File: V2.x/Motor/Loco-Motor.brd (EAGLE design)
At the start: 43.2 x 34.3 mm, 48 parts, among them IC1 Atmega 328-P, IC2 MCP2515, IC3 LM340MP-05, Q1 8MHz, Q2 16MHz

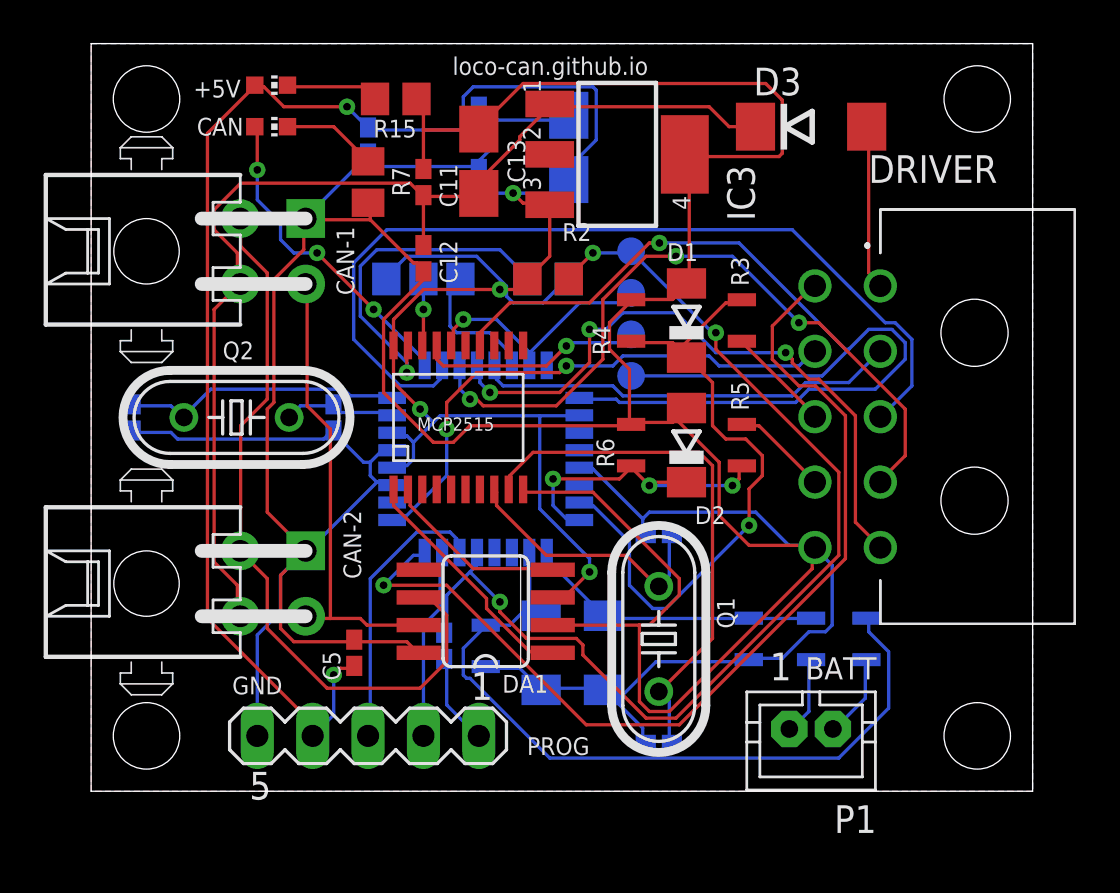
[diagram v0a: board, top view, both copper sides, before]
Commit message: changed sch and brd of motor and switch for RX/TX leds
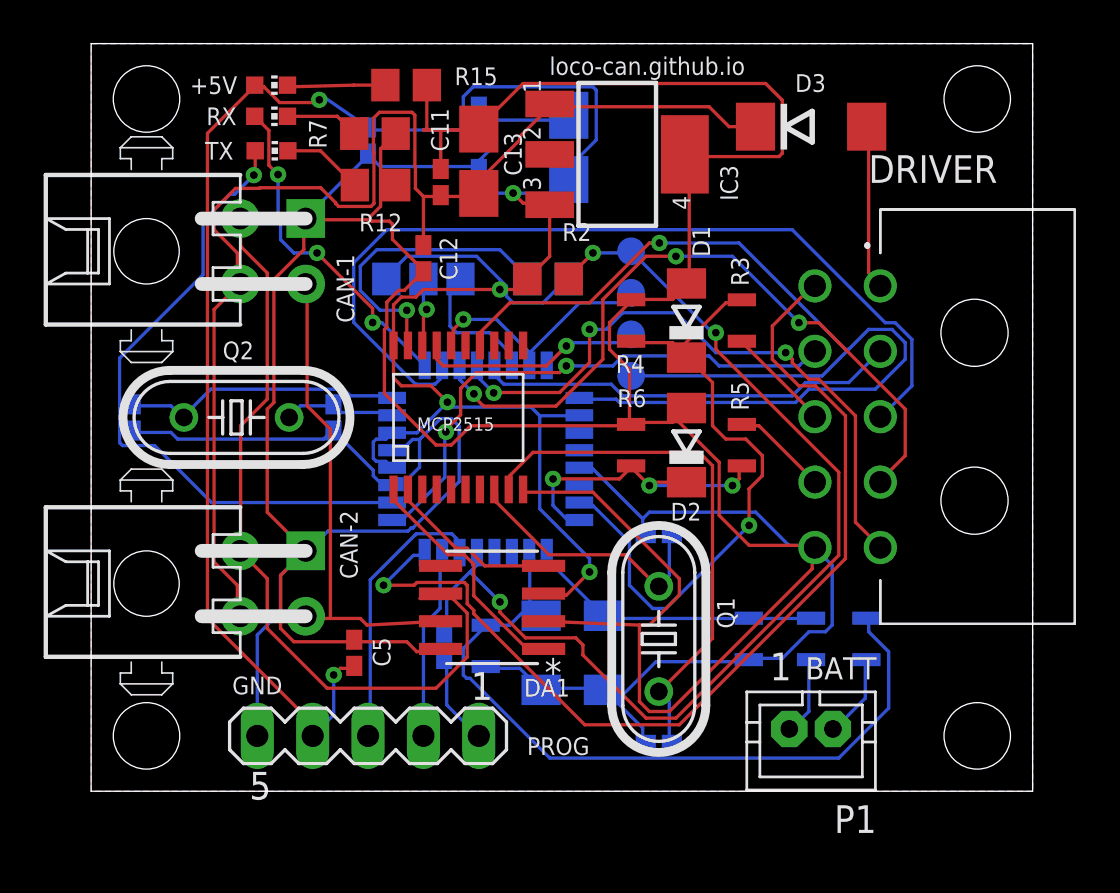
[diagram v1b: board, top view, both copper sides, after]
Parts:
- removed CAN: (no value), led:CHIP-LED0603
- added R12: 220R, rcl:R0805
- added RX, TX: (no value), led:CHIP-LED0603
- CAN-1, CAN-2: device SamacSys_Parts:SHDRRA4W102P300_2X2_686X892X73 -> Micro Mate-N-Lok:3-794618-4
- DA1: device TJA1050:SO08 -> MCP2551:SOIC8-N_MC_MCH
- IC2: device mcp2514:TSSOP20 -> MCP2515:TSSOP20
- PROG: device con-lstb:MA05-1 -> lst-b:MA05-1
- moved R7 2.25 mm to (13.0, 30.2), turned to 0 degrees
- moved C11 0.79 mm to (16.0, 27.9)
- moved R15 0.79 mm to (14.4, 32.4)
- moved DA1 0.34 mm to (18.4, 8.43), turned to 180 degrees
- renumbered SS to CS
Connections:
- removed net N$3: CAN.A, IC1.9
- new net D4: IC1.2, TX.A
- new net D5: IC1.9, RX.A
- new net N$4: R12.1, TX.C
- net GND: now also R12.2
- net N$2: now also RX.C; no longer CAN.C
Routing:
- net D4: track 0.00 -> 29.7 mm, vias 0 -> 1
- net GND: track 226.9 -> 244.6 mm
- net D5: track 0.00 -> 15.5 mm, vias 0 -> 3
- net N$3: track 14.9 -> 0.00 mm, vias 3 -> 0
- net +12V: track 50.8 -> 58.5 mm
- net N$4: track 0.00 -> 3.72 mm
- net CAN-L: track 33.9 -> 36.6 mm
- net VCC: track 115.7 -> 117.6 mm
- net N$6: track 15.6 -> 13.8 mm
- net CAN-H: track 21.2 -> 22.2 mm
- net N$2: track 4.36 -> 3.40 mm
- net D2: track 44.7 -> 45.4 mm
- net TXCAN: track 11.1 -> 11.7 mm
- net RXCAN: track 8.52 -> 7.95 mm
- net D6: track 41.7 -> 41.1 mm
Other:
- board text added: "ICP"
- board text removed: "ISP"
